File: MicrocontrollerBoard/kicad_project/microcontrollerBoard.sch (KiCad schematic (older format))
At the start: 49 parts, among them J1 PROG_CONN, J10 PC_5V, J11 CONN_RESET, J13 PA_GND, J14 PB_GND, J15 PC_GND, J18 COM, J19 COM_5V, J2 5V_CONN, J20 COM_GND, J21 POWER_CONN, J22 MOTOR2, J23 MOTOR1, J3 PA, J4 PB, J5 PC, J6 3V_CONN_1, J7 3V_CONN_2, J8 PA_5V, J9 PB_5V, U1 ATmega1284P-PU, U2 TC4422, U3 TC4422, U4 TC4422, U5 TC4422, U6 AMS1117-3.3, Y1 16MHz

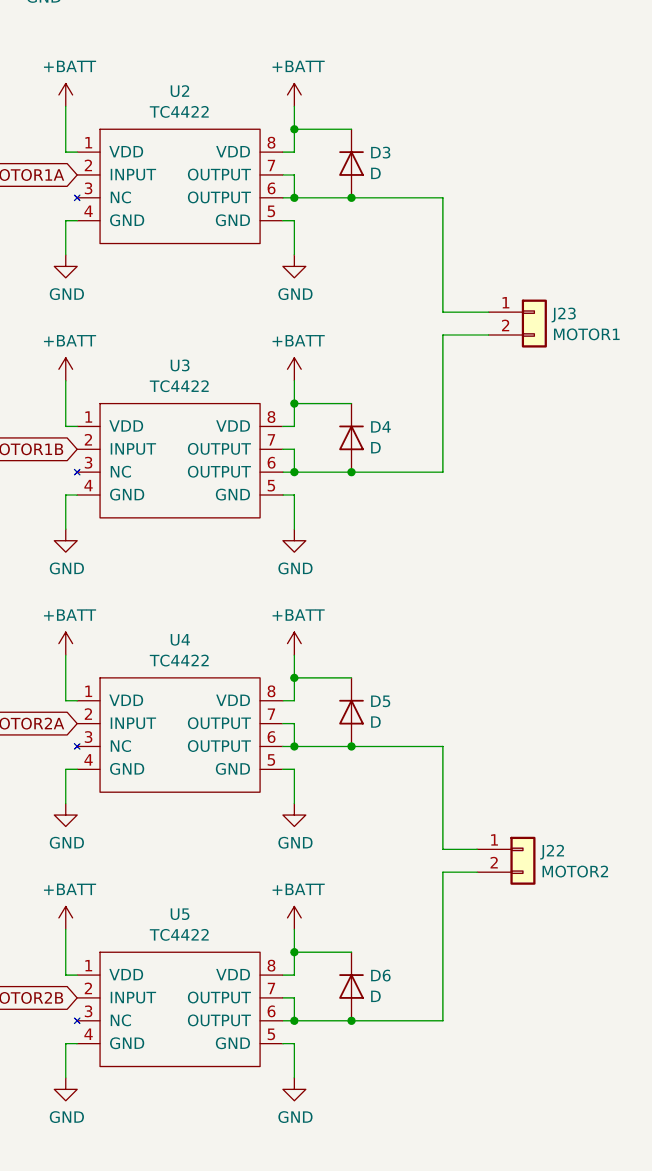
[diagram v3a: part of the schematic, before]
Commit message: uC board: Add motor diodes values (LL4148)
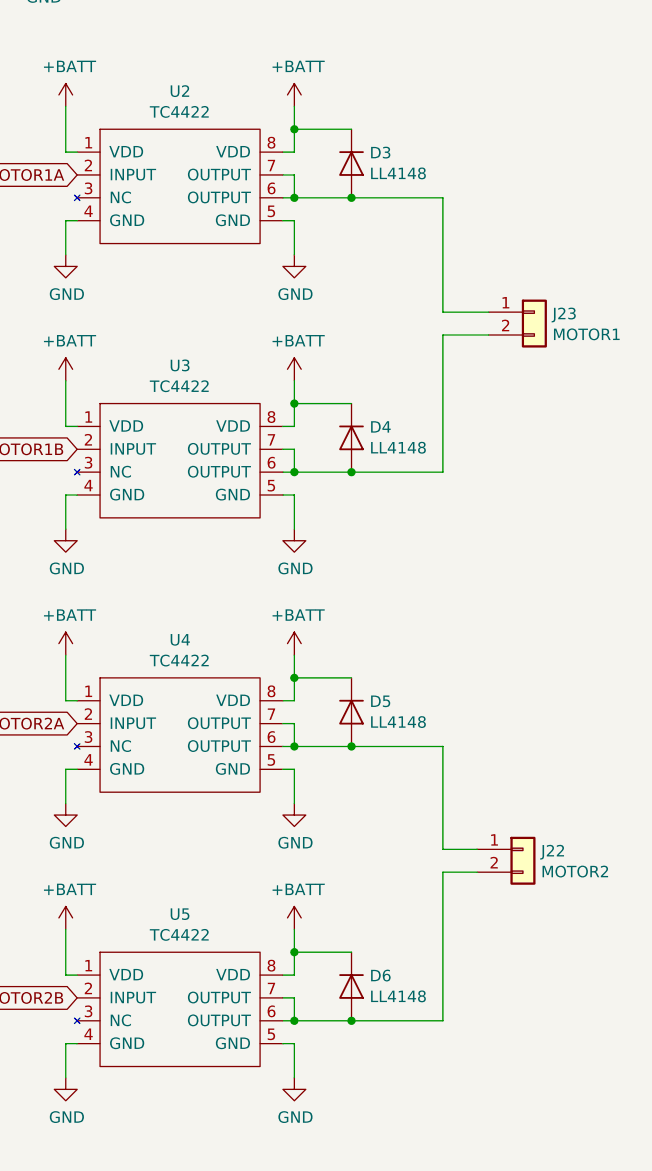
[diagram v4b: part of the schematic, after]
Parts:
- D3, D4, D5, D6: value D -> LL4148
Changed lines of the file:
@@
 P 9700 1950
 F 0 "D3" V 9654 2029 50  0000 L CNN
-F 1 "D" V 9745 2029 50  0000 L CNN
+F 1 "LL4148" V 9745 2029 50  0000 L CNN
 F 2 "Diode_SMD:D_SOD-110" H 9700 1950 50  0001 C CNN
 F 3 "~" H 9700 1950 50  0001 C CNN
@@
 P 9700 3150
 F 0 "D4" V 9654 3229 50  0000 L CNN
-F 1 "D" V 9745 3229 50  0000 L CNN
+F 1 "LL4148" V 9745 3229 50  0000 L CNN
 F 2 "Diode_SMD:D_SOD-110" H 9700 3150 50  0001 C CNN
 F 3 "~" H 9700 3150 50  0001 C CNN
@@
 P 9700 4350
 F 0 "D5" V 9654 4429 50  0000 L CNN
-F 1 "D" V 9745 4429 50  0000 L CNN
+F 1 "LL4148" V 9745 4429 50  0000 L CNN
 F 2 "Diode_SMD:D_SOD-110" H 9700 4350 50  0001 C CNN
 F 3 "~" H 9700 4350 50  0001 C CNN
@@
 P 9700 5550
 F 0 "D6" V 9654 5629 50  0000 L CNN
-F 1 "D" V 9745 5629 50  0000 L CNN
+F 1 "LL4148" V 9745 5629 50  0000 L CNN
 F 2 "Diode_SMD:D_SOD-110" H 9700 5550 50  0001 C CNN
 F 3 "~" H 9700 5550 50  0001 C CNN
